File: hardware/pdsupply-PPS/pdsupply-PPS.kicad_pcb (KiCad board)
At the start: 2 copper layers, 70 x 50 mm, 74 parts, among them IC1 LTM8083EY#PBF, IC2 FPF2895UCX, J1 USB4505-03-0-A_REVA, J2 USB4505-03-0-A_REVA, J3 Screw_Terminal_01x02, U1 FUSB307BMPX, U2 ADUM3160, U3 ACS71240KEXBLT-050U5, U4 STM32L432KCUx

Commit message: component placement done
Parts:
- moved TC1 112.0 mm to (146.2, 89.7), turned to -135 degrees
- moved C16 111.6 mm to (150.5, 102.5), turned to -135 degrees
- moved R17 109.2 mm to (151.5, 99.3), turned to -90 degrees
- moved C17 109.0 mm to (151.5, 96.3), turned to 90 degrees
- moved U3 106.9 mm to (123.3, 117.7), turned to 90 degrees
- moved U4 106.8 mm to (147.5, 98.0), turned to 180 degrees
- moved R18 105.9 mm to (148.1, 102.8), turned to -90 degrees
- moved U2 105.1 mm to (134.1, 89.0)
- moved D7 104.0 mm to (145.7, 102.0)
- moved C15 101.5 mm to (144.0, 94.5), turned to 45 degrees
- moved R16 100.0 mm to (145.7, 103.7), turned to 180 degrees
- moved R19 94.1 mm to (127.0, 116.2)
- moved C18 93.0 mm to (117.6, 115.1), turned to 90 degrees
- moved GPIO2 92.9 mm to (130.1, 111.7), turned to 90 degrees
- moved INT_N1 92.4 mm to (131.9, 111.7), turned to -90 degrees
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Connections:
- J3 pad 1: GND -> Net-(J3-Pad1)
- J3 pad 2: Net-(J3-Pad2) -> GND
- U3 pad 3: Net-(J3-Pad2) -> Net-(J3-Pad1)
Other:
- board size 70 x 50 mm -> 44 x 36.5 mm

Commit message: started layout
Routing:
- net +3V3: vias 0 -> 1
- added copper zone on In2.Cu, net +3V3
- added copper zone on In1.Cu, net GND
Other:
- copper layers 2 -> 4
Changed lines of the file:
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@@
 (kicad_pcb (version 20211014) (generator pcbnew)
   (general
-    (thickness 1.6)
+    (thickness 4.69)
   )
   (paper "A4")
   (layers
     (0 "F.Cu" signal)
+    (1 "In1.Cu" power)
+    (2 "In2.Cu" power)
     (31 "B.Cu" signal)
     (32 "B.Adhes" user "B.Adhesive")
@@
   )
   (setup
+    (stackup
+      (layer "F.SilkS" (type "Top Silk Screen"))
+      (layer "F.Paste" (type "Top Solder Paste"))
+      (layer "F.Mask" (type "Top Solder Mask") (thickness 0.01))
+      (layer "F.Cu" (type "copper") (thickness 0.035))
+      (layer "dielectric 1" (type "core") (thickness 1.51) (material "FR4") (epsilon_r 4.5) (loss_tangent 0.02))
+      (layer "In1.Cu" (type "copper") (thickness 0.035))
+      (layer "dielectric 2" (type "prepreg") (thickness 1.51) (material "FR4") (epsilon_r 4.5) (loss_tangent 0.02))
+      (layer "In2.Cu" (type "copper") (thickness 0.035))
+      (layer "dielectric 3" (type "core") (thickness 1.51) (material "FR4") (epsilon_r 4.5) (loss_tangent 0.02))
+      (layer "B.Cu" (type "copper") (thickness 0.035))
+      (layer "B.Mask" (type "Bottom Solder Mask") (thickness 0.01))
+      (layer "B.Paste" (type "Bottom Solder Paste"))
+      (layer "B.SilkS" (type "Bottom Silk Screen"))
+      (copper_finish "None")
+      (dielectric_constraints no)
+    )
     (pad_to_mask_clearance 0)
     (aux_axis_origin 110 120)
@@
   (gr_line (start 152.992893 105.792893) (end 146.007107 105.807107) (layer "Edge.Cuts") (width 0.1))
   (gr_arc (start 111.007107 119.992893) (mid 110.3 119.7) (end 110.007107 118.992893) (layer "Edge.Cuts") (width 0.1))
+  (via (at 140.1 102.2) (size 0.8) (drill 0.4) (layers "F.Cu" "B.Cu") (net 1))
+  (zone (net 4) (net_name "GND") (layer "In1.Cu") (hatch edge 0.508)
+    (connect_pads (clearance 0.508))
+    (min_thickness 0.254) (filled_areas_thickness no)
+    (fill yes (thermal_gap 0.508) (thermal_bridge_width 0.508))
+    (polygon
+      (pts
+        (xy 154.3 106.6)
+        (xy 146.1 106.7)
+        (xy 146 121)
+        (xy 109 121)
+        (xy 109.4 83)
+        (xy 154.3 82.7)
+      )
+    )
+  )
+  (zone (net 1) (net_name "+3V3") (layer "In2.Cu") (hatch edge 0.508)
+    (connect_pads (clearance 0.508))
+    (min_thickness 0.254) (filled_areas_thickness no)
+    (fill yes (thermal_gap 0.508) (thermal_bridge_width 0.508))
+    (polygon
+      (pts
+        (xy 154.380911 106.6)
+        (xy 146.180911 106.7)
+        (xy 146.080911 121)
+        (xy 109.080911 121)
+        (xy 109.480911 83)
+        (xy 154.380911 82.7)
+      )
+    )
+  )
 )

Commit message: added few routes
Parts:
- C4, C5, D1, D2: moved to B.Cu
- moved +5V1 5.91 mm to (113.8, 89.7)
- moved C18 3.30 mm to (120.5, 116.6)
- moved D1 2.41 mm to (120.7, 107.8)
- moved D2 2.41 mm to (120.7, 104.8)
- moved C13 2.37 mm to (119.2, 116.6), turned to 90 degrees
- moved C4 1.56 mm to (119.1, 107.8)
- moved C5 1.56 mm to (119.1, 104.8)
- moved CC1 0.51 mm to (122.7, 108.8)
- moved GPIO1 0.14 mm to (124.4, 105.8)
- turned R1 to -90 degrees
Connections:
- net Net-(C13-Pad1) renamed /Vbus_pre
- net Net-(J3-Pad1) renamed /VBus_Out
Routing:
- net GND1: track 0.00 -> 39.5 mm, vias 0 -> 3
- net GND: track 0.00 -> 35.1 mm, vias 0 -> 64
- net +5V: track 0.00 -> 24.9 mm, vias 0 -> 4
- net +3V3: track 0.00 -> 19.6 mm, vias 1 -> 5
- net Net-(JP1-Pad1): track 0.00 -> 18.9 mm, vias 0 -> 2
- net Net-(JP2-Pad1): track 0.00 -> 13.9 mm, vias 0 -> 2
- net Net-(C6-Pad1): track 0.00 -> 11.2 mm
- net /CC1: track 0.00 -> 10.7 mm, vias 0 -> 2
- net /CC2: track 0.00 -> 9.19 mm, vias 0 -> 2
- net VBUS: track 0.00 -> 8.20 mm
- net Net-(C11-Pad1): track 0.00 -> 7.66 mm
- net Net-(D7-Pad1): track 0.00 -> 2.28 mm
- net Net-(IC1-PadB6): track 0.00 -> 1.91 mm
- net Net-(R18-Pad1): track 0.00 -> 1.91 mm
- net Net-(D7-Pad2): track 0.00 -> 1.76 mm
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- added copper zone on F.Cu, net /Vbus_pre
- added copper zone on F.Cu, net GND
- added copper zone on F.Cu, net VBUS

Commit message: almost done with routing
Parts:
- moved SCL1 1.50 mm to (140.8, 97.1)
- moved SDA1 1.50 mm to (140.8, 98.8)
- moved USB_DP1 0.30 mm to (141.6, 93.3)
- moved R4 0.17 mm to (128.7, 107.1)
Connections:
- net Net-(C8-Pad1) renamed /+3.3V_Pre
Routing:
- net /DBG_N: track 0.00 -> 47.7 mm, vias 0 -> 4
- net /SenseFault: track 0.00 -> 43.7 mm, vias 0 -> 2
- net /Isense: track 0.00 -> 42.8 mm, vias 0 -> 2
- net /FLAGB: track 0.00 -> 37.6 mm, vias 0 -> 2
- net /VSINK_EN: track 0.00 -> 36.5 mm, vias 0 -> 2
- net /USB_DP: track 0.00 -> 35.2 mm, vias 0 -> 4
- net /INT_N: track 0.00 -> 31.6 mm, vias 0 -> 2
- net /USB_DM: track 0.00 -> 29.8 mm, vias 0 -> 4
- net /SCL: track 0.00 -> 28.6 mm, vias 0 -> 2
- net /SDA: track 0.00 -> 27.0 mm, vias 0 -> 2
- net +3V3: track 19.6 -> 44.4 mm, vias 5 -> 19
- net GND: track 35.1 -> 53.4 mm, vias 64 -> 93
- net Net-(D6-Pad1): track 1.52 -> 10.7 mm
- net Net-(IC1-PadF7): track 0.00 -> 7.25 mm
- net Net-(IC1-PadE7): track 0.00 -> 6.03 mm
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- added copper zone on F.Cu, net +3V3
- added copper zone on F.Cu, net /+3.3V_Pre
- added copper zone on F.Cu, net /VBus_Out
- added copper zone on B.Cu, net /Vbus_pre

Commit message: almost done
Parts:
- added H1: MountingHole_Pad, MountingHole:MountingHole_3mm, F.Cu at (112.0, 118.1)
- added H2: MountingHole_Pad, MountingHole:MountingHole_3mm, F.Cu at (112.0, 85.6)
- added H3: MountingHole_Pad, MountingHole:MountingHole_3mm, F.Cu at (173.9, 117.4)
- added H4: MountingHole_Pad, MountingHole:MountingHole_3mm, F.Cu at (152.0, 85.6)
- moved TC1 1.90 mm to (146.4, 87.9), turned to -90 degrees
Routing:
- net /FLAGB: track 37.6 -> 58.7 mm, vias 2 -> 3
- net Net-(R17-Pad2): track 0.00 -> 2.86 mm
- net GND: track 53.4 -> 54.4 mm
- net /Vbus_pre: vias 28 -> 16

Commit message: added holes
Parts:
- removed H3: MountingHole_Pad, MountingHole:MountingHole_3mm
- removed R1: 200k, Resistor_SMD:R_0603_1608Metric
- removed R2: 270k, Resistor_SMD:R_0603_1608Metric
- H1, H2, H4: footprint MountingHole:MountingHole_3mm -> MountingHole:MountingHole_3mm_Pad
- moved DBG_N1 10.5 mm to (140.8, 104.8), turned to 135 degrees
- moved D5 10.3 mm to (130.5, 96.3)
- moved R14 10.3 mm to (130.5, 94.8)
- moved C6 4.25 mm to (124.1, 102.0), turned to -90 degrees
- moved J1 3.27 mm to (108.4, 106.2)
- moved FLAGB1 2.67 mm to (132.8, 96.0)
- moved SenseFault1 2.67 mm to (136.2, 96.0)
- moved VSINK_EN1 2.67 mm to (134.5, 96.0)
- moved H1 2.46 mm to (110.1, 116.5)
- moved H4 2.19 mm to (153.8, 86.9)
- moved H2 2.11 mm to (110.3, 86.9)
- moved Isense1 0.82 mm to (137.7, 96.1)
- moved J2 0.59 mm to (121.5, 84.5)
- moved R11 0.59 mm to (120.7, 93.2)
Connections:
- C6 pad 1: Net-(C6-Pad1) -> /VBUS_Rdy
- FB1 pad 2: Net-(C6-Pad1) -> /VBUS_Rdy
- FB2 pad 2: Net-(C6-Pad1) -> /VBUS_Rdy
- IC1 pad A1: GND -> Net-(IC1-PadA1)
- IC1 pad A2: GND -> Net-(IC1-PadA1)
- IC1 pad A3: GND -> Net-(IC1-PadA1)
- IC1 pad A4: Net-(C6-Pad1) -> /VBUS_Rdy
- IC1 pad A5: Net-(C6-Pad1) -> /VBUS_Rdy
- IC1 pad A6: Net-(C6-Pad1) -> /VBUS_Rdy
- IC1 pad A7: GND -> Net-(IC1-PadA1)
- IC1 pad B1: GND -> Net-(IC1-PadA1)
- IC1 pad B2: GND -> Net-(IC1-PadA1)
- IC1 pad B3: GND -> Net-(IC1-PadA1)
- IC1 pad B4: Net-(C6-Pad1) -> /VBUS_Rdy
- IC1 pad B5: Net-(C6-Pad1) -> /VBUS_Rdy
- IC1 pad B6: Net-(IC1-PadB6) -> /VBUS_Rdy
- IC1 pad B7: GND -> Net-(IC1-PadA1)
- IC1 pad C1: GND -> Net-(IC1-PadA1)
- IC1 pad C2: GND -> Net-(IC1-PadA1)
- IC1 pad C3: GND -> Net-(IC1-PadA1)
- IC1 pad C4: GND -> Net-(IC1-PadA1)
- IC1 pad C5: GND -> Net-(IC1-PadA1)
- IC1 pad D1: GND -> Net-(IC1-PadA1)
- IC1 pad D2: GND -> Net-(IC1-PadA1)
- IC1 pad D3: GND -> Net-(IC1-PadA1)
- IC1 pad D4: GND -> Net-(IC1-PadA1)
- IC1 pad D5: GND -> Net-(IC1-PadA1)
- IC1 pad D7: GND -> Net-(IC1-PadA1)
- IC1 pad E1: GND -> Net-(IC1-PadA1)
- IC1 pad E2: GND -> Net-(IC1-PadA1)
- IC1 pad E3: GND -> Net-(IC1-PadA1)
- IC1 pad E4: GND -> Net-(IC1-PadA1)
- IC1 pad E5: GND -> Net-(IC1-PadA1)
- IC1 pad F1: GND -> Net-(IC1-PadA1)
- IC1 pad F2: GND -> Net-(IC1-PadA1)
- IC1 pad G1: GND -> Net-(IC1-PadA1)
- IC1 pad G2: GND -> Net-(IC1-PadA1)
- IC1 pad G6: GND -> Net-(IC1-PadA1)
- R3 pad 2: GND -> Net-(IC1-PadA1)
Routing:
- net Net-(TC1-Pad2): track 0.00 -> 39.1 mm, vias 0 -> 2
- net Net-(TC1-Pad4): track 0.00 -> 36.7 mm
- net /Isense: track 42.8 -> 70.4 mm, vias 2 -> 3
- net Net-(R17-Pad2): track 2.86 -> 28.1 mm, vias 0 -> 2
- net /VSINK_EN: track 36.5 -> 59.9 mm, vias 2 -> 4
- net /SenseFault: track 43.7 -> 61.5 mm, vias 2 -> 3
- net Net-(IC1-PadA1): track 0.00 -> 8.71 mm, vias 0 -> 6
- net +3V3: track 43.9 -> 52.4 mm
- net VBUS: track 11.2 -> 3.80 mm
- net Net-(C6-Pad1): track 7.07 -> 0.00 mm
- net /DBG_N: track 47.7 -> 51.6 mm
- net GND1: track 43.7 -> 39.9 mm
- net /CC2: track 9.19 -> 12.5 mm
- net /CC1: track 10.7 -> 14.0 mm
- net Net-(JP1-Pad1): track 18.9 -> 16.9 mm
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- added copper zone on F.Cu, net /VBUS_Rdy
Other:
- board size 44 x 36.5 mm -> 50.5 x 37.1 mm

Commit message: layout done!
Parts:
- R11, R12: moved to B.Cu
- moved R11 1.63 mm to (122.3, 93.2)
- moved R12 1.63 mm to (120.7, 92.6)
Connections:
- IC1 pad A1: Net-(IC1-PadA1) -> GND
- IC1 pad A2: Net-(IC1-PadA1) -> GND
- IC1 pad A3: Net-(IC1-PadA1) -> GND
- IC1 pad A7: Net-(IC1-PadA1) -> GND
- IC1 pad B1: Net-(IC1-PadA1) -> GND
- IC1 pad B2: Net-(IC1-PadA1) -> GND
- IC1 pad B3: Net-(IC1-PadA1) -> GND
- IC1 pad B7: Net-(IC1-PadA1) -> GND
- IC1 pad C1: Net-(IC1-PadA1) -> GND
- IC1 pad C2: Net-(IC1-PadA1) -> GND
- IC1 pad C3: Net-(IC1-PadA1) -> GND
- IC1 pad C4: Net-(IC1-PadA1) -> GND
- IC1 pad C5: Net-(IC1-PadA1) -> GND
- IC1 pad D1: Net-(IC1-PadA1) -> GND
- IC1 pad D2: Net-(IC1-PadA1) -> GND
- IC1 pad D3: Net-(IC1-PadA1) -> GND
- IC1 pad D4: Net-(IC1-PadA1) -> GND
- IC1 pad D5: Net-(IC1-PadA1) -> GND
- IC1 pad D7: Net-(IC1-PadA1) -> GND
- IC1 pad E1: Net-(IC1-PadA1) -> GND
- IC1 pad E2: Net-(IC1-PadA1) -> GND
- IC1 pad E3: Net-(IC1-PadA1) -> GND
- IC1 pad E4: Net-(IC1-PadA1) -> GND
- IC1 pad E5: Net-(IC1-PadA1) -> GND
- IC1 pad F1: Net-(IC1-PadA1) -> GND
- IC1 pad F2: Net-(IC1-PadA1) -> GND
- IC1 pad G1: Net-(IC1-PadA1) -> GND
- IC1 pad G2: Net-(IC1-PadA1) -> GND
- IC1 pad G6: Net-(IC1-PadA1) -> GND
- R3 pad 2: Net-(IC1-PadA1) -> GND
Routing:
- net GND1: track 39.9 -> 58.9 mm, vias 2 -> 4
- net Net-(J2-PadA6): track 0.00 -> 12.1 mm, vias 0 -> 2
- net Net-(IC1-PadA1): track 8.71 -> 0.00 mm, vias 6 -> 0
- net +5V: track 24.2 -> 31.2 mm
- net Net-(J2-PadA7): track 2.23 -> 7.83 mm, vias 0 -> 1
- net GND: track 54.1 -> 59.6 mm, vias 88 -> 90
- net Net-(JP2-Pad1): track 14.2 -> 19.2 mm
- net Net-(JP1-Pad1): track 16.9 -> 18.6 mm
- net unconnected-(U3-Pad10): track 0.00 -> 1.50 mm
- net Net-(D4-Pad1): track 6.90 -> 6.48 mm, vias 2 -> 0

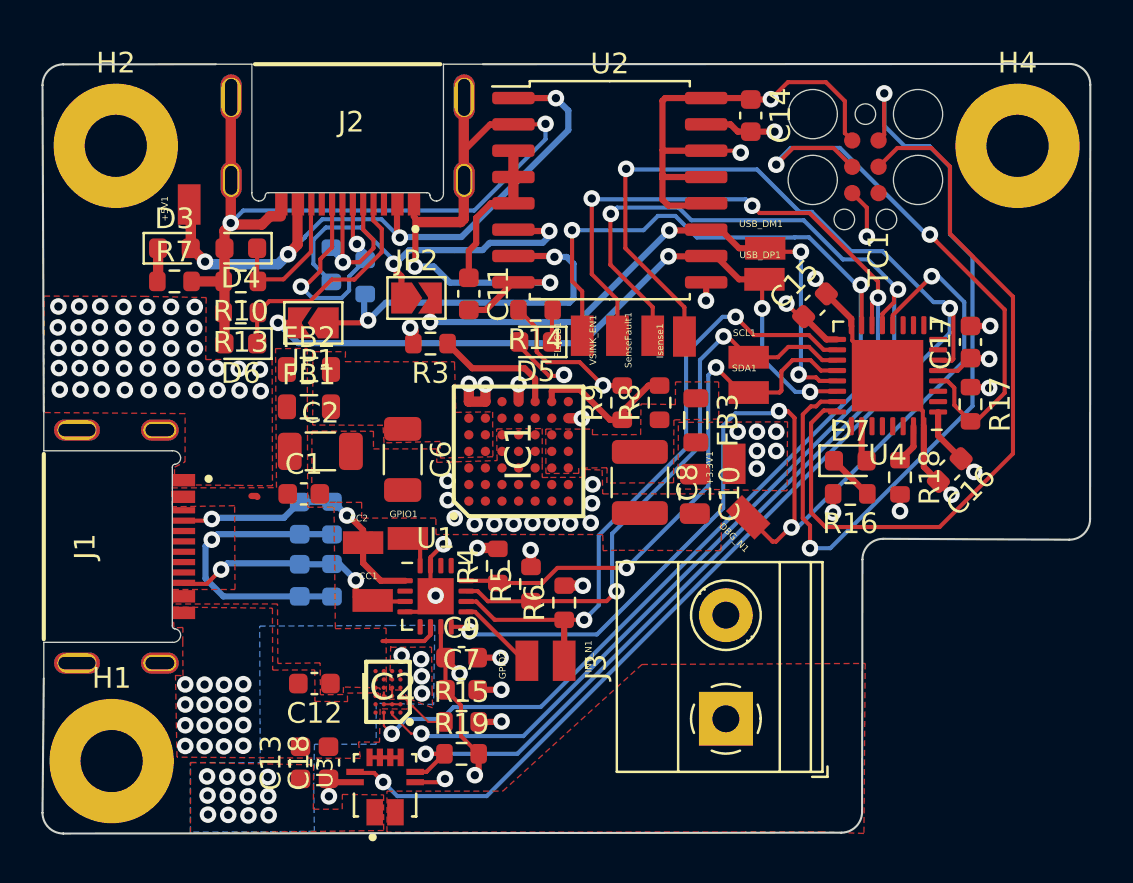
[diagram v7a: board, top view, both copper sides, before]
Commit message: Removed ref Designators
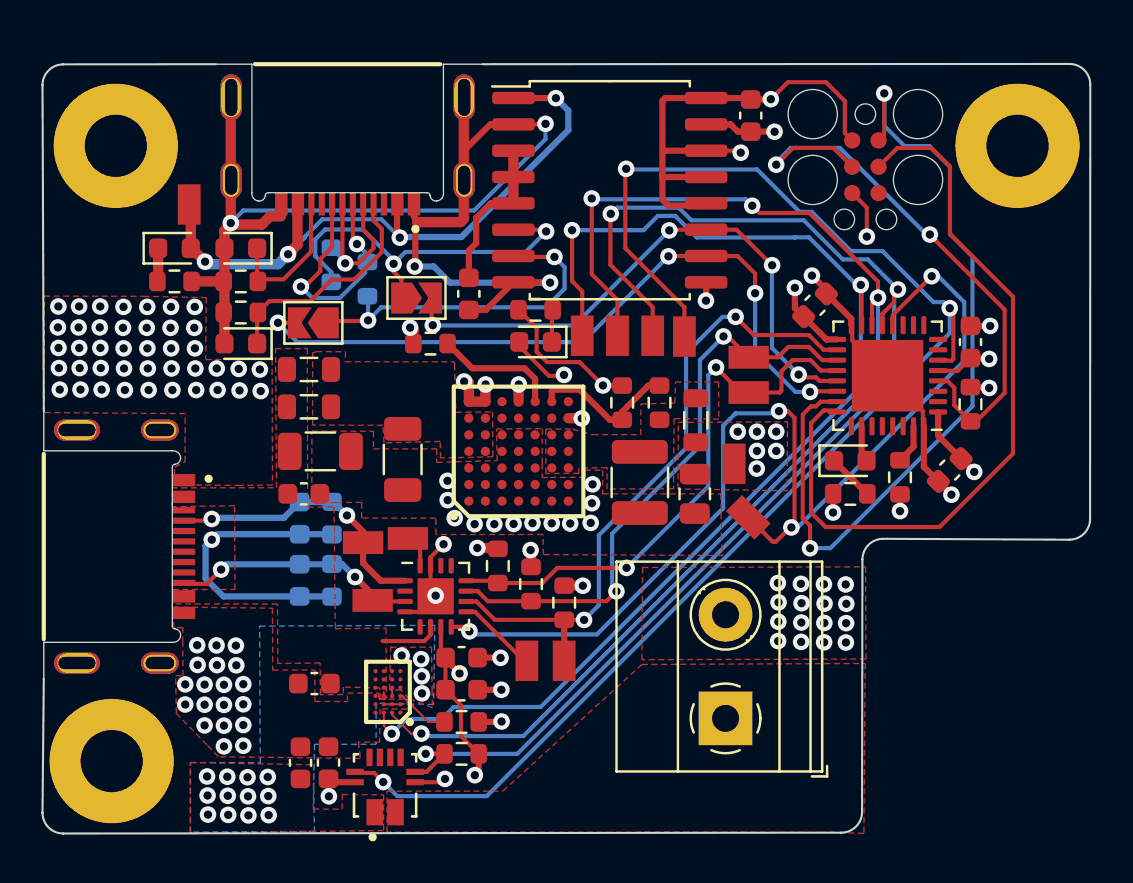
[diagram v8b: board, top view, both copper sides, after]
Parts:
- removed USB_DM1, USB_DP1: RCU-0C, RCU-0C:TP+195X110
- moved R11 0.15 mm to (122.4, 93.3)
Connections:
- U3 pad 7: unconnected-(U3-Pad10) -> unconnected-(U3-Pad7)
- U3 pad 8: unconnected-(U3-Pad10) -> unconnected-(U3-Pad8)
- U3 pad 9: unconnected-(U3-Pad10) -> unconnected-(U3-Pad9)
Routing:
- net Net-(JP1-Pad1): track 18.6 -> 16.9 mm
- net /USB_DM: track 29.8 -> 28.2 mm
- net unconnected-(U3-Pad10): track 1.50 -> 0.00 mm
- net /CC1: track 14.0 -> 13.4 mm
- net GND: track 59.6 -> 59.7 mm, vias 90 -> 109
